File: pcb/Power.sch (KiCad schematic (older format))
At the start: 25 parts, among them J11 CONN_01X02, J12 CONN_01X04, Q1 Q_PMOS_GDS, U1 REG-LM317, U2 REG-7805, U3 LD1086-3.3

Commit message: hoskins.tech
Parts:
- D1, D2, D3, D4: symbol LED -> LED-RESCUE-TFCB
- D5, D6: symbol D -> D-RESCUE-TFCB
- Q1: symbol Q_PMOS_GDS -> Q_PMOS_GDS-RESCUE-TFCB

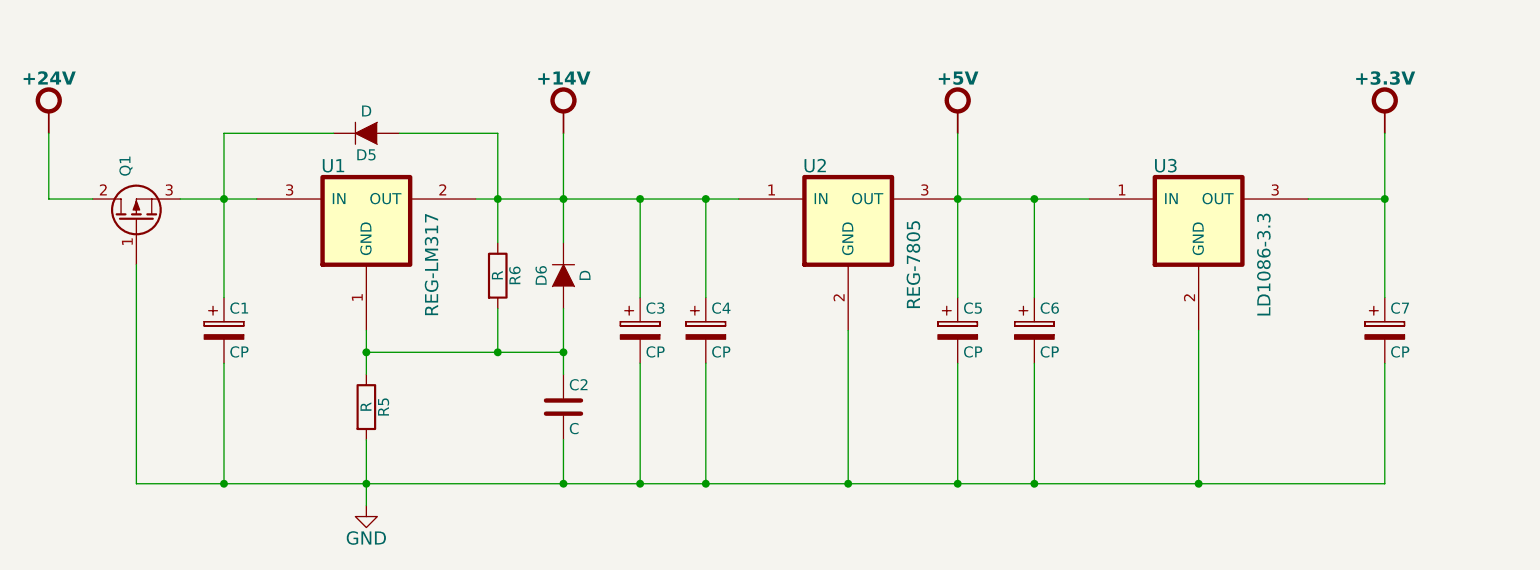
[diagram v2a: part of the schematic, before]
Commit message: Moved power regulators to top side and corrected bad package
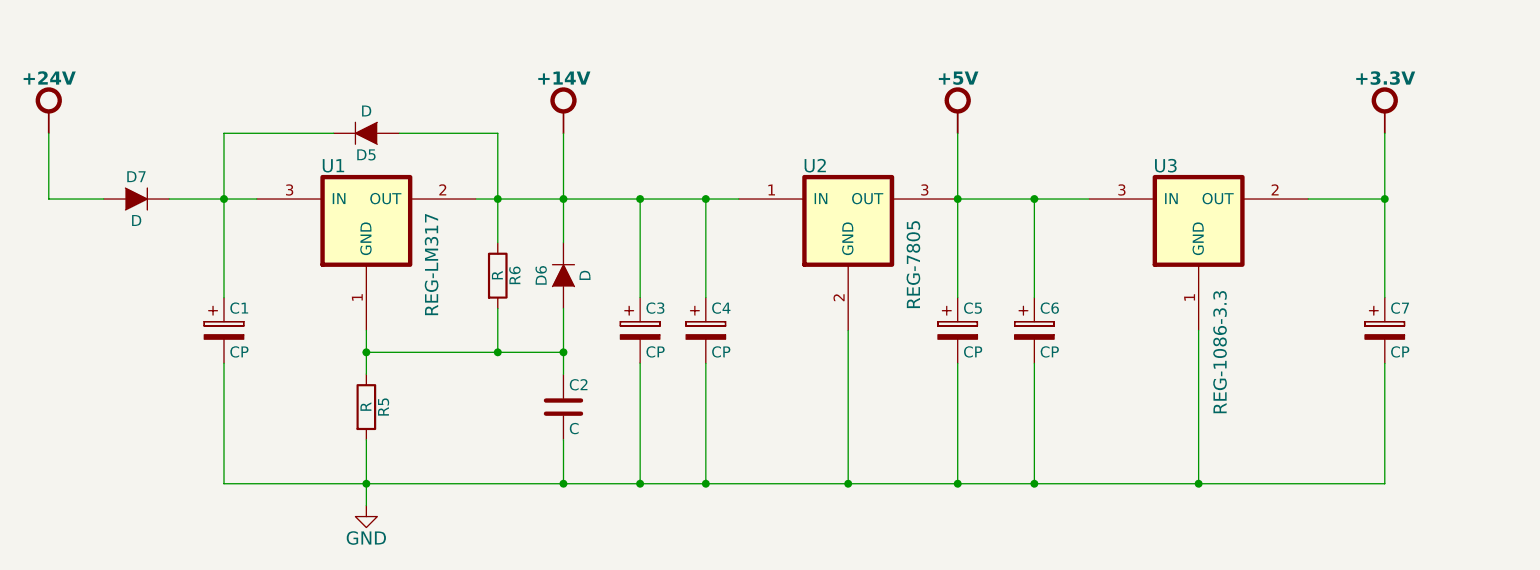
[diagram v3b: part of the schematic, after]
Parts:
- removed Q1: Q_PMOS_GDS, bjh-kicad-transistor-fp:TO-263, symbol Q_PMOS_GDS-RESCUE-TFCB
- removed U3: LD1086-3.3, bjh-kicad-transistor-fp:TO-263, symbol LD1086-3.3
- added D7: D, Diodes_SMD:DO-214AB_Handsoldering, symbol D-RESCUE-TFCB
- added U3: REG-1086-3.3, bjh-kicad-transistor-fp:TO-263, symbol REG-LM317
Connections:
- net +24V: now also D7.1 (A)
- net +3.3V: now also U3.2 (OUT)
- net +5V: now also U3.3 (IN)
- net GND: now also U3.1 (GND)
- net at C1.1, D5.2 (K), U1.3 (IN): now also D7.2 (K)
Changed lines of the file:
@@
 LIBS:contrib
 LIBS:valves
-LIBS:transistors_gaui
-LIBS:transistor-fet
 LIBS:TFCB-cache
 EELAYER 25 0
@@
 $EndDescr
 $Comp
-L Q_PMOS_GDS-RESCUE-TFCB Q1
-U 1 1 5507406A
-P 1050 6300
-F 0 "Q1" H 1350 6350 50  0000 R CNN
-F 1 "Q_PMOS_GDS" H 1700 6250 50  0001 R CNN
-F 2 "bjh-kicad-transistor-fp:TO-263" H 1250 6400 29  0001 C CNN
-F 3 "" H 1050 6300 60  0000 C CNN
-	1    1050 6300
-	0    -1   -1   0
-$EndComp
-$Comp
 L R R5
 U 1 1 550741A2
@@
 $EndComp
 $Comp
-L LD1086-3.3 U3
-U 1 1 5507E6C6
-P 5400 6200
-F 0 "U3" H 5750 6350 60  0000 C CNN
-F 1 "LD1086-3.3" V 6200 5900 60  0000 C CNN
-F 2 "bjh-kicad-transistor-fp:TO-263" H 5400 6200 60  0001 C CNN
-F 3 "" H 5400 6200 60  0000 C CNN
-	1    5400 6200
-	1    0    0    -1
-$EndComp
-$Comp
 L CP C6
 U 1 1 5507E701
@@
 	1    0    0    -1
 $EndComp
-Wire Wire Line
-	1600 6200 1250 6200
-Wire Wire Line
-	2100 6800 2100 7000
-Wire Wire Line
-	2100 7300 2100 7600
-Wire Wire Line
-	2700 6700 2700 6900
-Wire Wire Line
-	2100 6900 3000 6900
-Connection ~ 2100 6900
-Wire Wire Line
-	2700 5900 2700 6400
-Wire Wire Line
-	3000 5900 3000 6400
-Connection ~ 2700 6200
-Wire Wire Line
-	3000 6700 3000 7000
-Connection ~ 2700 6900
-Connection ~ 3000 6900
-Wire Wire Line
-	3000 7500 3000 7300
-Connection ~ 1450 6200
-Wire Wire Line
-	1050 7500 6750 7500
-Connection ~ 2100 7500
-Wire Wire Line
-	1050 6500 1050 7500
-Connection ~ 1450 7500
-Wire Wire Line
-	1450 5900 1450 6650
-Wire Wire Line
-	1450 6950 1450 7500
-Wire Wire Line
-	3350 6200 3350 6650
-Connection ~ 3000 6200
-Wire Wire Line
-	3350 7500 3350 6950
-Connection ~ 3000 7500
-Wire Wire Line
-	1950 5900 1450 5900
-Wire Wire Line
-	2250 5900 2700 5900
-Wire Wire Line
-	3650 6200 3650 6650
-Connection ~ 3350 6200
-Wire Wire Line
-	3650 7500 3650 6950
-Connection ~ 3350 7500
-Connection ~ 3650 6200
-Connection ~ 3650 7500
-Wire Wire Line
-	4800 5900 4800 6650
-Wire Wire Line
-	4800 7500 4800 6950
-Wire Wire Line
-	2600 6200 3800 6200
-Wire Wire Line
-	4300 6800 4300 7500
-Connection ~ 4300 7500
-Connection ~ 4800 6200
-Wire Wire Line
-	650  6200 850  6200
-Wire Wire Line
-	650  5900 650  6200
-Wire Wire Line
-	4800 6200 5400 6200
-Wire Wire Line
-	5150 6650 5150 6200
-Connection ~ 5150 6200
-Wire Wire Line
-	6750 5900 6750 6650
-Wire Wire Line
-	6750 6200 6400 6200
-Wire Wire Line
-	6750 7500 6750 6950
-Connection ~ 4800 7500
-Wire Wire Line
-	5150 6950 5150 7500
-Connection ~ 5150 7500
-Wire Wire Line
-	5900 6800 5900 7500
-Connection ~ 5900 7500
-Connection ~ 6750 6200
-Wire Wire Line
-	1150 1300 1150 1400
-Wire Wire Line
-	1450 1300 1450 1400
-Wire Wire Line
-	1750 1300 1750 1400
-Wire Wire Line
-	2050 1300 2050 1400
-Wire Wire Line
-	1150 1800 1150 1900
-Wire Wire Line
-	2050 1900 2050 1800
-Wire Wire Line
-	1600 1900 1600 1950
-Connection ~ 1600 1900
-Wire Wire Line
-	1750 1900 1750 1800
-Connection ~ 1750 1900
-Wire Wire Line
-	1450 1800 1450 1900
-Connection ~ 1450 1900
-Wire Wire Line
-	1150 1000 1150 950
-Wire Wire Line
-	1450 1000 1450 950
-Wire Wire Line
-	1750 1000 1750 950
-Wire Wire Line
-	2050 1000 2050 950
-Connection ~ 2050 1900
-Wire Wire Line
-	10550 900  10650 900
-Wire Wire Line
-	10550 1050 10550 1000
-Wire Wire Line
-	10550 1000 10650 1000
-Wire Wire Line
-	10500 1750 10500 1850
-Wire Wire Line
-	10500 1850 10650 1850
-Wire Wire Line
-	10250 1750 10250 1950
-Wire Wire Line
-	10250 1950 10650 1950
-Wire Wire Line
-	10000 1750 10000 2050
-Wire Wire Line
-	10000 2050 10650 2050
-Wire Wire Line
-	10550 2200 10550 2150
-Wire Wire Line
-	10550 2150 10650 2150
-Wire Wire Line
-	1150 1900 2050 1900
-Wire Wire Line
-	10550 850  10550 900
 $Comp
 L +24V_BJH #PWR016
@@
 	1    0    0    -1
 $EndComp
+$Comp
+L REG-LM317 U3
+U 1 1 56126E48
+P 5700 6100
+F 0 "U3" H 5750 6150 60  0000 C CNN
+F 1 "REG-1086-3.3" V 6000 5300 60  0000 C CNN
+F 2 "bjh-kicad-transistor-fp:TO-263" H 5400 6000 60  0001 C CNN
+F 3 "" H 5400 6000 60  0000 C CNN
+	1    5700 6100
+	1    0    0    -1
+$EndComp
+Wire Wire Line
+	1200 6200 1600 6200
+Wire Wire Line
+	2100 6800 2100 7000
+Wire Wire Line
+	2100 7300 2100 7600
+Wire Wire Line
+	2700 6700 2700 6900
+Wire Wire Line
+	2100 6900 3000 6900
+Connection ~ 2100 6900
+Wire Wire Line
+	2700 5900 2700 6400
+Wire Wire Line
+	3000 5900 3000 6400
+Connection ~ 2700 6200
+Wire Wire Line
+	3000 6700 3000 7000
+Connection ~ 2700 6900
+Connection ~ 3000 6900
+Wire Wire Line
+	3000 7500 3000 7300
+Connection ~ 1450 6200
+Wire Wire Line
+	1450 7500 6750 7500
+Connection ~ 2100 7500
+Wire Wire Line
+	1450 5900 1450 6650
+Wire Wire Line
+	1450 6950 1450 7500
+Wire Wire Line
+	3350 6200 3350 6650
+Connection ~ 3000 6200
+Wire Wire Line
+	3350 7500 3350 6950
+Connection ~ 3000 7500
+Wire Wire Line
+	1950 5900 1450 5900
+Wire Wire Line
+	2250 5900 2700 5900
+Wire Wire Line
+	3650 6200 3650 6650
+Connection ~ 3350 6200
+Wire Wire Line
+	3650 7500 3650 6950
+Connection ~ 3350 7500
+Connection ~ 3650 6200
+Connection ~ 3650 7500
+Wire Wire Line
+	4800 5900 4800 6650
+Wire Wire Line
+	4800 7500 4800 6950
+Wire Wire Line
+	2600 6200 3800 6200
+Wire Wire Line
+	4300 6800 4300 7500
+Connection ~ 4300 7500
+Connection ~ 4800 6200
+Wire Wire Line
+	650  6200 900  6200
+Wire Wire Line
+	650  5900 650  6200
+Wire Wire Line
+	4800 6200 5400 6200
+Wire Wire Line
+	5150 6650 5150 6200
+Connection ~ 5150 6200
+Wire Wire Line
+	6750 5900 6750 6650
+Wire Wire Line
+	6750 6200 6400 6200
+Wire Wire Line
+	6750 7500 6750 6950
+Connection ~ 4800 7500
+Wire Wire Line
+	5150 6950 5150 7500
+Connection ~ 5150 7500
+Wire Wire Line
+	5900 6800 5900 7500
+Connection ~ 5900 7500
+Connection ~ 6750 6200
+Wire Wire Line
+	1150 1300 1150 1400
+Wire Wire Line
+	1450 1300 1450 1400
+Wire Wire Line
+	1750 1300 1750 1400
+Wire Wire Line
+	2050 1300 2050 1400
+Wire Wire Line
+	1150 1800 1150 1900
+Wire Wire Line
+	2050 1900 2050 1800
+Wire Wire Line
+	1600 1900 1600 1950
+Connection ~ 1600 1900
+Wire Wire Line
+	1750 1900 1750 1800
+Connection ~ 1750 1900
+Wire Wire Line
+	1450 1800 1450 1900
+Connection ~ 1450 1900
+Wire Wire Line
+	1150 1000 1150 950
+Wire Wire Line
+	1450 1000 1450 950
+Wire Wire Line
+	1750 1000 1750 950
+Wire Wire Line
+	2050 1000 2050 950
+Connection ~ 2050 1900
+Wire Wire Line
+	10550 900  10650 900
+Wire Wire Line
+	10550 1050 10550 1000
+Wire Wire Line
+	10550 1000 10650 1000
+Wire Wire Line
+	10500 1750 10500 1850
+Wire Wire Line
+	10500 1850 10650 1850
+Wire Wire Line
+	10250 1750 10250 1950
+Wire Wire Line
+	10250 1950 10650 1950
+Wire Wire Line
+	10000 1750 10000 2050
+Wire Wire Line
+	10000 2050 10650 2050
+Wire Wire Line
+	10550 2200 10550 2150
+Wire Wire Line
+	10550 2150 10650 2150
+Wire Wire Line
+	1150 1900 2050 1900
+Wire Wire Line
+	10550 850  10550 900
+$Comp
+L D-RESCUE-TFCB D7
+U 1 1 56263237
+P 1050 6200
+F 0 "D7" H 1050 6300 50  0000 C CNN
+F 1 "D" H 1050 6100 50  0000 C CNN
+F 2 "Diodes_SMD:DO-214AB_Handsoldering" H 1050 6200 60  0001 C CNN
+F 3 "" H 1050 6200 60  0000 C CNN
+	1    1050 6200
+	1    0    0    -1
+$EndComp
